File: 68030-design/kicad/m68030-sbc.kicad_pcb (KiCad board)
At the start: 4 copper layers, 220 x 175 mm, 292 parts, among them J1 SIMM-72 socket, J10 DIN41612-C-96, J11 LA1 A31-A0, J12 LA2 D31-D0, J13 LA3 control, J2 9-24V DC, J3 5V_BENCH, J4 JTAG (ATDH1150USB), J5 JTAG U4 (ATDH1150USB), J6 IDE 40-pin, J7 TTL-232, J8 TTL-232, J9 SPI NIC, Q1 SUD50P04-08, SW1 WARM_RESET, SW2 NMI, SW3 COLD_RESET, U1 MC68030RC33C, U10 74ACT244, U11 SN74ACT245DW, U12 SN74ACT245DW, U13 SN74ACT245DW, U14 SN74ACT244DW, U15 SN74ACT244DW, U16 SN74ACT244DW, U17 SN74ACT244DW, U18 SN74ACT245DW, U19 SN74ACT245DW, U2 MC68882FN33A, U20 SN74ACT245DW, U21 SN74ACT245DW, U22 SN74LVC125ADR, U23 DS3234S#, U27 TPS3808G50DBVR, U3 ATF1508AS-7JX84, U4 ATF1508AS-7JX84, U5 SST39SF040-70-4C-NHE, U6 SC26C92A1A, U7 TPS3702CX50DDCR, U8 LM2678S-5.0, U801 74ACT257, U802 74ACT257, U803 74ACT257, U9 AMS1117-3.3, X1 25.000MHz, X2 50.000MHz, X3 FPU osc (DNP), Y1 3.6864MHz

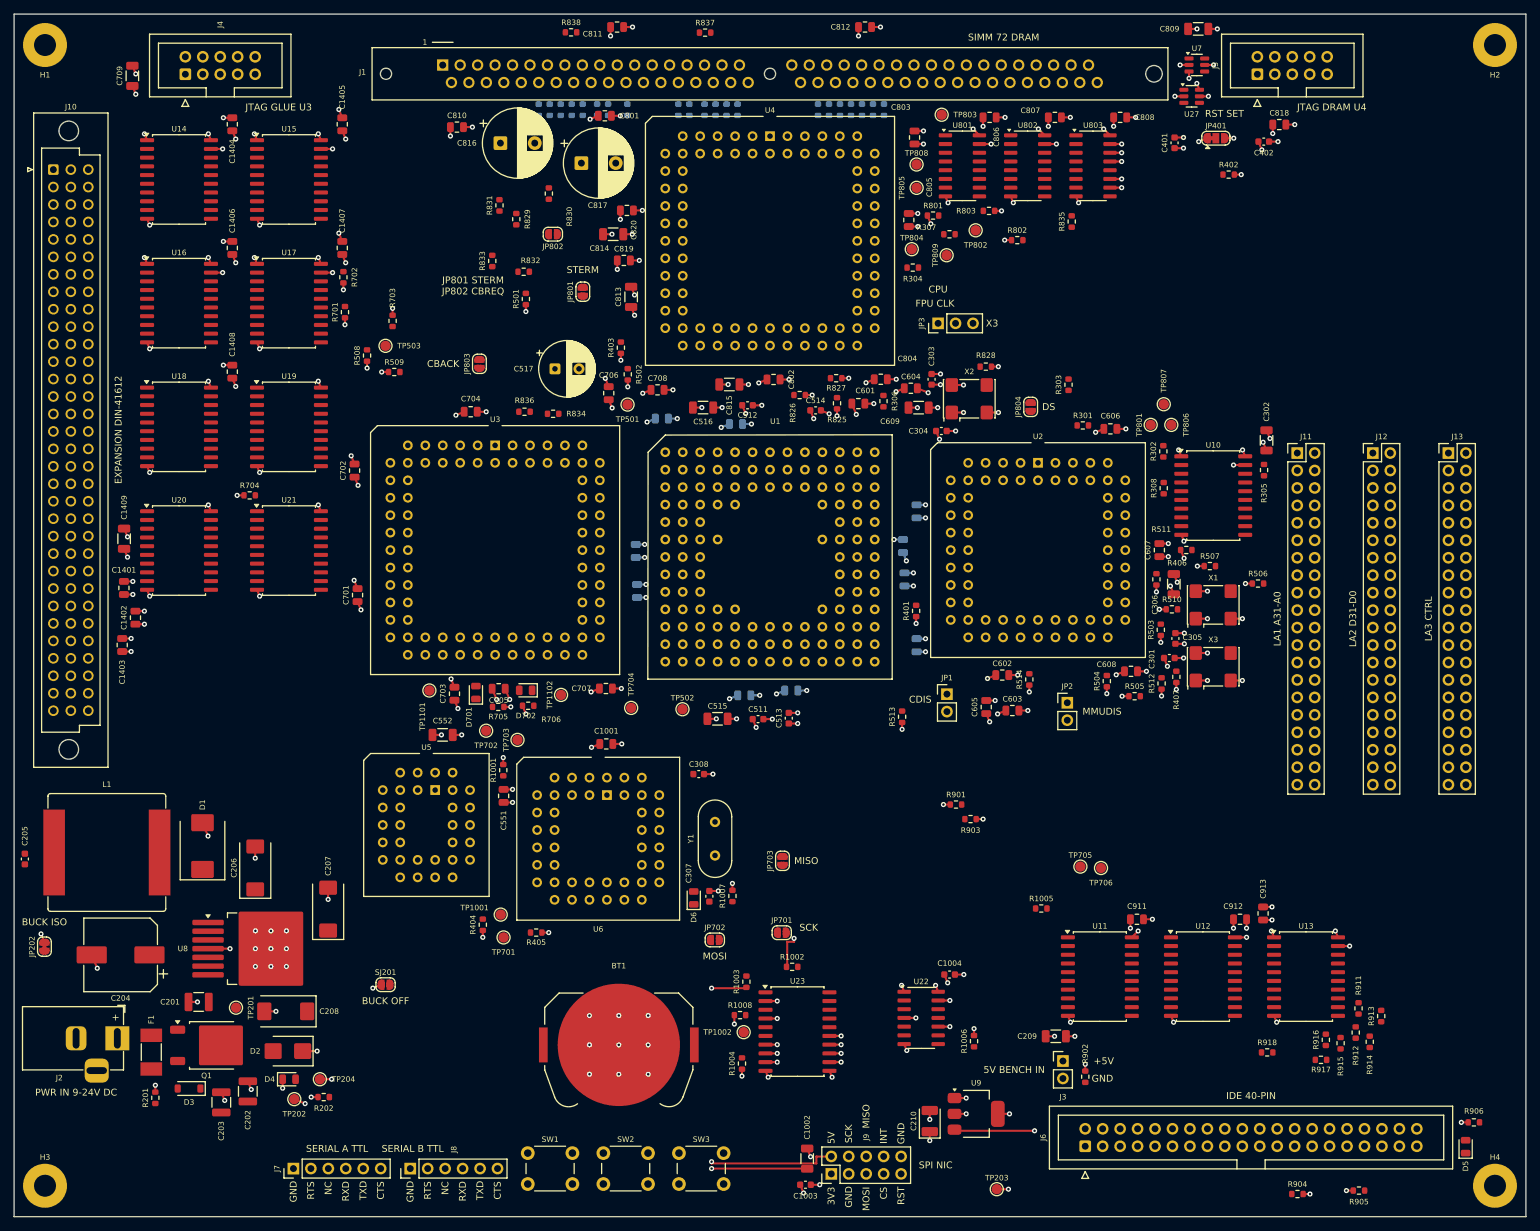
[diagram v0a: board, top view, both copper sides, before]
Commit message: PCB: fully route the 4-layer board, then fix DRAM termination, strobe stubs and clocks
Route all 499 signal connections on the 220x175 mm 4-layer board, with signals
on F.Cu/B.Cu and solid In1 GND / In2 +5V (+3V3 island). The scripted grid router
is in kicad/tools/route/ (0.4233 mm grid aligned to U1, A* + PathFinder).
Then fix signal integrity (kicad/tools/route/sifix/): strip the signal tracks,
move the parts and reroute.

Full route (first pass):
- 100 % routed, DRC 0 errors, parity 0; 2453 vias, 56.1 m of signal track.
- 55 parts nudged <= 0.212 mm onto the grid. The DNP 74ACT257 fallback
  (U801-U803, R829-R838) is set to on_board no in dram.kicad_sch.

SI fix (this board, sha1 2221a671):
- DRAM 33R R804-R824 moved to B.Cu next to U4: pad to U4 pin is now
  1.6-6.9 mm (was 2.9-27.2 mm).
- RAS0_n/CAS3_n/WE_n: LA3 J13 pins 37-39 are now NC (debug.kicad_sch).
  TP801/806/807 moved to the SIMM-side resistors.
  RAS0_n 325/17 -> 27.5 mm/1 via, CAS3_n 232/7 -> 17.8/0, WE_n 224/5 -> 17.4/1.
  TP stubs are 0 / 13.5 / 9.7 mm.
- Clock block (U10, X1, R301-R306, decaps) moved next to U4/U3. R307/R308 moved
  to the X2/X3 outputs. U10 outputs swapped in clock.kicad_sch: pin 18 CLKB_DRAMC,
  pin 14 CLKB_CPU, pin 12 CLKB_GLUE.
  CLK_EXP 147/2 -> 56/0, CLK_GLUE 109/0 -> 22/0, CLK_CPU 75/2 -> 57/0,
  CLK_DRAMC 38 -> 62, CLK_FPU_CPU 52/2 -> 70/0, DRAM_CLK 37 -> 59/0,
  X2-OUT 31/2 -> 4/0. Every CLKB_* is 1.7 mm. Clocks are ~100 % on F.Cu over GND.
  Tradeoff: CLK_LA 28 -> 202 mm/2 vias, CLKB_X3 (DNP) 51 -> 80 mm.
- Board total: 2365 vias, 53.8 m of signal track. 100 % routed, DRC 0 errors,
  0 unconnected, parity 0, ERC 0/0. 4 silk warnings (was 5). .kicad_pro unchanged.
- Note: build.py / sheet_*.py do not contain the J13 NC or the U10 swap.
- Renders: renders/m68030-sbc-routed-*.png, renders/m68030-sbc-sifix-*.png.
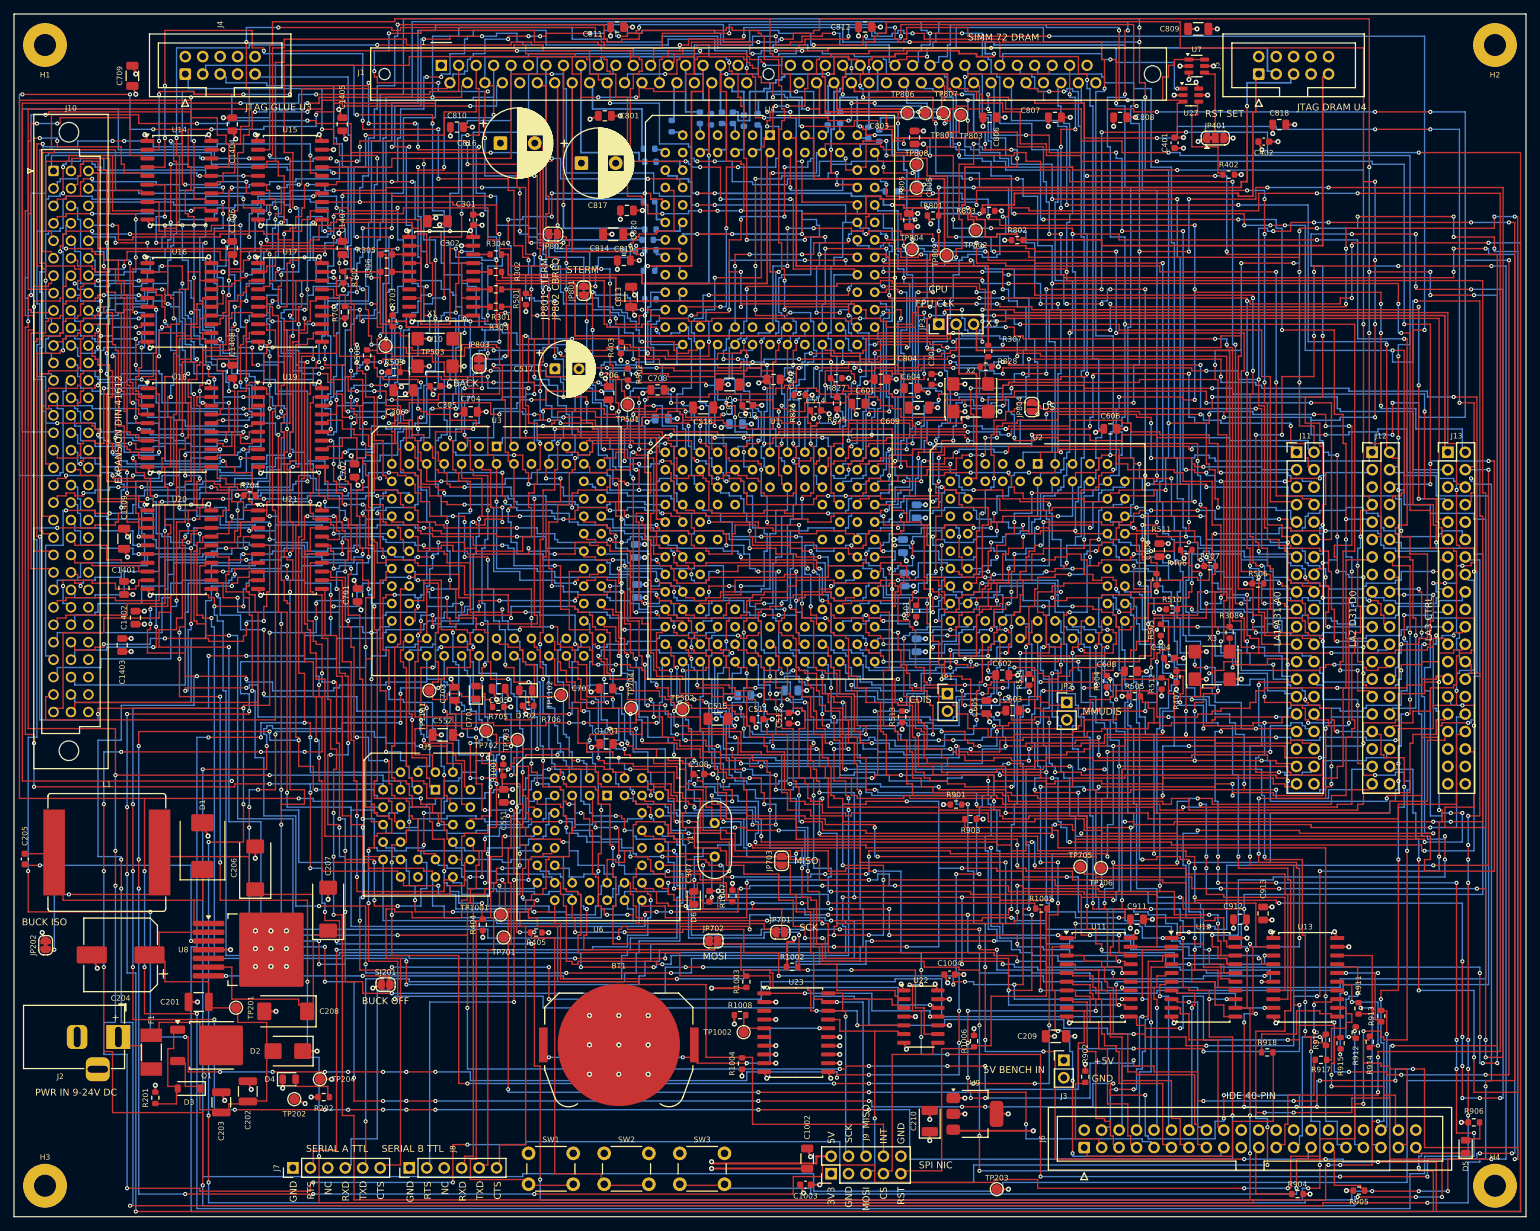
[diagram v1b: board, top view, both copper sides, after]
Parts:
- removed R829, R830, R831, R832, R833, R834, R835, R836, R837, R838: 33, Resistor_SMD:R_0603_1608Metric
- removed U801, U802, U803: 74ACT257, Package_SO:SOIC-16_3.9x9.9mm_P1.27mm
- moved R305 131.5 mm to (54.2, 35.0), turned to 180 degrees
- moved C302 124.7 mm to (61.7, 30.1), turned to 0 degrees
- moved X1 119.1 mm to (61.3, 49.2)
- moved C301 119.0 mm to (66.8, 29.9)
- moved U10 116.8 mm to (62.2, 38.1)
- moved C306 115.6 mm to (56.7, 54.7), turned to 0 degrees
- moved C305 113.9 mm to (61.3, 54.1)
- moved R302 100.6 mm to (70.1, 37.5), turned to 0 degrees
- moved R301 87.7 mm to (70.1, 40.1)
- moved R303 84.1 mm to (70.1, 42.6), turned to 0 degrees
- moved R306 74.7 mm to (54.2, 37.5), turned to 180 degrees
- moved R304 60.7 mm to (70.1, 35.0)
- moved TP806 59.4 mm to (130.0, 14.4)
- moved TP807 54.8 mm to (132.6, 14.4)
- moved TP801 54.5 mm to (135.2, 14.4)
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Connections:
- J13 pad 37: /RAS0_n -> unconnected-(J13-Pin_37-Pad37)
- J13 pad 38: /CAS3_n -> unconnected-(J13-Pin_38-Pad38)
- J13 pad 39: /WE_n -> unconnected-(J13-Pin_39-Pad39)
- U10 pad 12: /clock/CLKB_DRAMC -> /clock/CLKB_GLUE
- U10 pad 14: /clock/CLKB_GLUE -> /clock/CLKB_CPU
- U10 pad 18: /clock/CLKB_CPU -> /clock/CLKB_DRAMC
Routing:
- net /A8: track 0.00 -> 855.1 mm, vias 0 -> 46
- net /A17: track 0.00 -> 843.7 mm, vias 0 -> 30
- net /D18: track 0.00 -> 778.5 mm, vias 0 -> 35
- net /D21: track 0.00 -> 759.9 mm, vias 0 -> 47
- net /A19: track 0.00 -> 756.5 mm, vias 0 -> 30
- net /A5: track 0.00 -> 745.9 mm, vias 0 -> 20
- net /A6: track 0.00 -> 737.9 mm, vias 0 -> 26
- net /A12: track 0.00 -> 736.6 mm, vias 0 -> 20
- net /D12: track 0.00 -> 736.2 mm, vias 0 -> 32
- net /D22: track 0.00 -> 729.8 mm, vias 0 -> 20
- net /A9: track 0.00 -> 700.2 mm, vias 0 -> 30
- net /D31: track 0.00 -> 690.9 mm, vias 0 -> 26
- net /R_W: track 0.00 -> 664.2 mm, vias 0 -> 38
- net /D5: track 0.00 -> 663.8 mm, vias 0 -> 33
- net /D0: track 0.00 -> 663.8 mm, vias 0 -> 34
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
